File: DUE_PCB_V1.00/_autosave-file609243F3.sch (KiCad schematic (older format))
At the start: 24 parts, among them J26 Motor_Left2, J37 RPM_Mow, J38 ODO_Left, J39 ODO_Right, J40 Motor_Right, J41 Motor_Left, J42 Cutter, J7 Motor_Right2, U1 MC33926, U2 MC33926

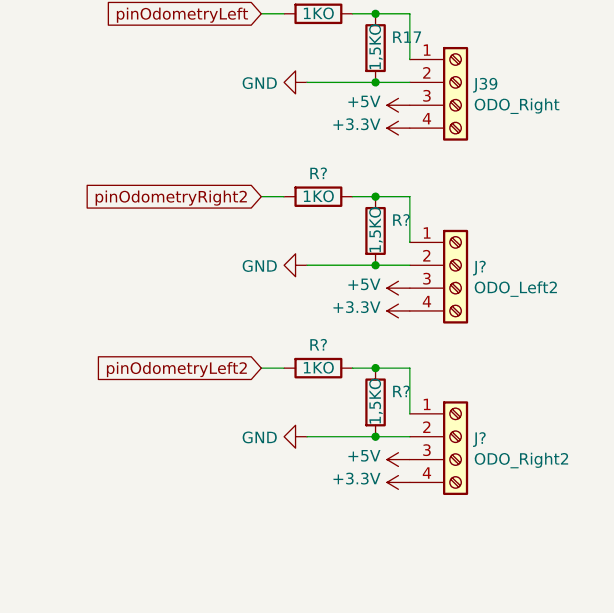
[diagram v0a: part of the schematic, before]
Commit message: Add 2 new Motor Connectors and Odo
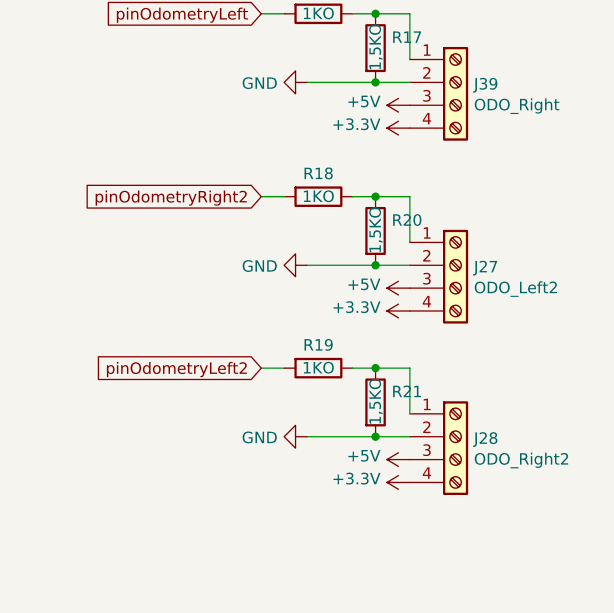
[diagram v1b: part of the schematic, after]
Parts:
- gave numbers to parts that had none: 6
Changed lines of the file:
@@
 Connection ~ 1000 3700
 $Comp
-L Connector:Screw_Terminal_01x04 J?
+L Connector:Screw_Terminal_01x04 J27
 U 1 1 60BA8B67
 P 8400 3550
-F 0 "J?" H 8480 3542 50  0000 L CNN
+F 0 "J27" H 8480 3542 50  0000 L CNN
 F 1 "ODO_Left2" H 8480 3451 50  0000 L CNN
 F 2 "Connector_PinHeader_2.54mm:PinHeader_1x04_P2.54mm_Vertical" H 8400 3550 50  0001 C CNN
@@
 $EndComp
 $Comp
-L power:+3.3V #PWR?
+L power:+3.3V #PWR064
 U 1 1 60BA8F67
 P 8200 3750
-F 0 "#PWR?" H 8200 3600 50  0001 C CNN
+F 0 "#PWR064" H 8200 3600 50  0001 C CNN
 F 1 "+3.3V" V 8215 3878 50  0000 L CNN
 F 2 "" H 8200 3750 50  0001 C CNN
@@
 pinOdometryRight2
 $Comp
-L Connector:Screw_Terminal_01x04 J?
+L Connector:Screw_Terminal_01x04 J28
 U 1 1 60BA8F72
 P 8400 4300
-F 0 "J?" H 8480 4292 50  0000 L CNN
+F 0 "J28" H 8480 4292 50  0000 L CNN
 F 1 "ODO_Right2" H 8480 4201 50  0000 L CNN
 F 2 "Connector_PinHeader_2.54mm:PinHeader_1x04_P2.54mm_Vertical" H 8400 4300 50  0001 C CNN
@@
 $EndComp
 $Comp
-L power:+3.3V #PWR?
+L power:+3.3V #PWR095
 U 1 1 60BA8F7C
 P 8200 4500
-F 0 "#PWR?" H 8200 4350 50  0001 C CNN
+F 0 "#PWR095" H 8200 4350 50  0001 C CNN
 F 1 "+3.3V" V 8215 4628 50  0000 L CNN
 F 2 "" H 8200 4500 50  0001 C CNN
@@
 $EndComp
 $Comp
-L power:+5V #PWR?
+L power:+5V #PWR081
 U 1 1 60BA8F86
 P 8200 4400
-F 0 "#PWR?" H 8200 4250 50  0001 C CNN
+F 0 "#PWR081" H 8200 4250 50  0001 C CNN
 F 1 "+5V" V 8215 4528 50  0000 L CNN
 F 2 "" H 8200 4400 50  0001 C CNN
@@
 pinOdometryLeft2
 $Comp
-L power:+5V #PWR?
+L power:+5V #PWR063
 U 1 1 60BA8F91
 P 8200 3650
-F 0 "#PWR?" H 8200 3500 50  0001 C CNN
+F 0 "#PWR063" H 8200 3500 50  0001 C CNN
 F 1 "+5V" V 8215 3778 50  0000 L CNN
 F 2 "" H 8200 3650 50  0001 C CNN
@@
 $EndComp
 $Comp
-L power:GND #PWR?
+L power:GND #PWR061
 U 1 1 60BA8F9B
 P 7750 4300
-F 0 "#PWR?" H 7750 4050 50  0001 C CNN
+F 0 "#PWR061" H 7750 4050 50  0001 C CNN
 F 1 "GND" V 7755 4172 50  0000 R CNN
 F 2 "" H 7750 4300 50  0001 C CNN
@@
 $EndComp
 $Comp
-L Device:R R?
+L Device:R R21
 U 1 1 60BA8FA5
 P 8050 4150
-F 0 "R?" H 8120 4196 50  0000 L CNN
+F 0 "R21" H 8120 4196 50  0000 L CNN
 F 1 "1,5KO" V 8050 4050 50  0000 L CNN
 F 2 "Resistor_THT:R_Axial_DIN0207_L6.3mm_D2.5mm_P2.54mm_Vertical" V 7980 4150 50  0001 C CNN
@@
 $EndComp
 $Comp
-L Device:R R?
+L Device:R R19
 U 1 1 60BA8FAF
 P 7800 4000
-F 0 "R?" V 7700 4000 50  0000 C CNN
+F 0 "R19" V 7700 4000 50  0000 C CNN
 F 1 "1KO" V 7800 4000 50  0000 C CNN
 F 2 "Resistor_THT:R_Axial_DIN0207_L6.3mm_D2.5mm_P2.54mm_Vertical" V 7730 4000 50  0001 C CNN
@@
 Connection ~ 8050 4300
 $Comp
-L power:GND #PWR?
+L power:GND #PWR060
 U 1 1 60BA8FC0
 P 7750 3550
-F 0 "#PWR?" H 7750 3300 50  0001 C CNN
+F 0 "#PWR060" H 7750 3300 50  0001 C CNN
 F 1 "GND" V 7755 3422 50  0000 R CNN
 F 2 "" H 7750 3550 50  0001 C CNN
@@
 $EndComp
 $Comp
-L Device:R R?
+L Device:R R20
 U 1 1 60BA8FCA
 P 8050 3400
-F 0 "R?" H 8120 3446 50  0000 L CNN
+F 0 "R20" H 8120 3446 50  0000 L CNN
 F 1 "1,5KO" V 8050 3300 50  0000 L CNN
 F 2 "Resistor_THT:R_Axial_DIN0207_L6.3mm_D2.5mm_P2.54mm_Vertical" V 7980 3400 50  0001 C CNN
@@
 $EndComp
 $Comp
-L Device:R R?
+L Device:R R18
 U 1 1 60BA8FD4
 P 7800 3250
-F 0 "R?" V 7700 3250 50  0000 C CNN
+F 0 "R18" V 7700 3250 50  0000 C CNN
 F 1 "1KO" V 7800 3250 50  0000 C CNN
 F 2 "Resistor_THT:R_Axial_DIN0207_L6.3mm_D2.5mm_P2.54mm_Vertical" V 7730 3250 50  0001 C CNN
